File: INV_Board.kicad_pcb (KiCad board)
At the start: 2 copper layers, 100 x 50 mm, 109 parts, among them J1 USB_B_Micro, J10 Conn_01x02_Male, J11 Conn_01x04_Male, J2 Conn_01x02_Male, J3 Conn_01x02_Male, J4 Conn_01x02_Male, J5 Conn_01x04_Male, J6 Conn_01x03_Male, J7 Conn_01x03_Male, J8 Conn_ARM_JTAG_SWD_10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

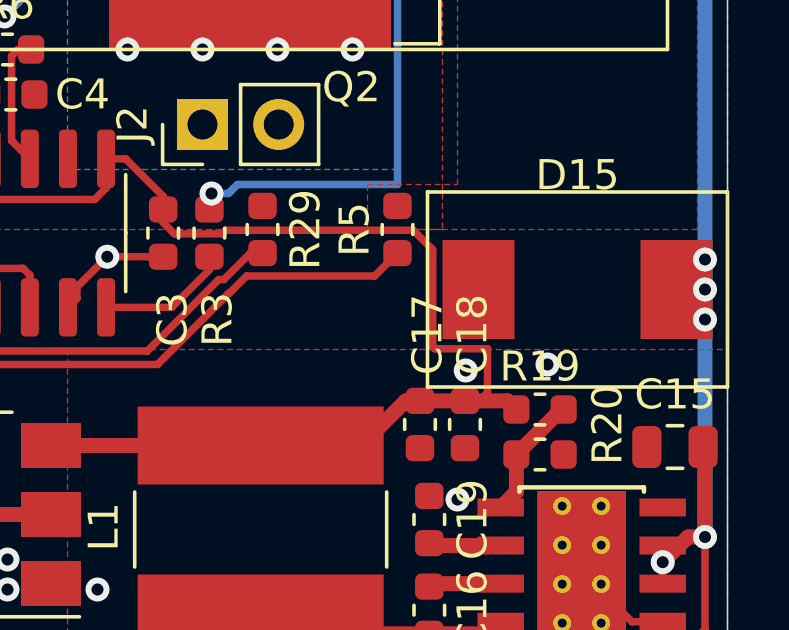
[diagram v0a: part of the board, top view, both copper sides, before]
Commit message: Commit changes to put omitted Vias on TVS ground.
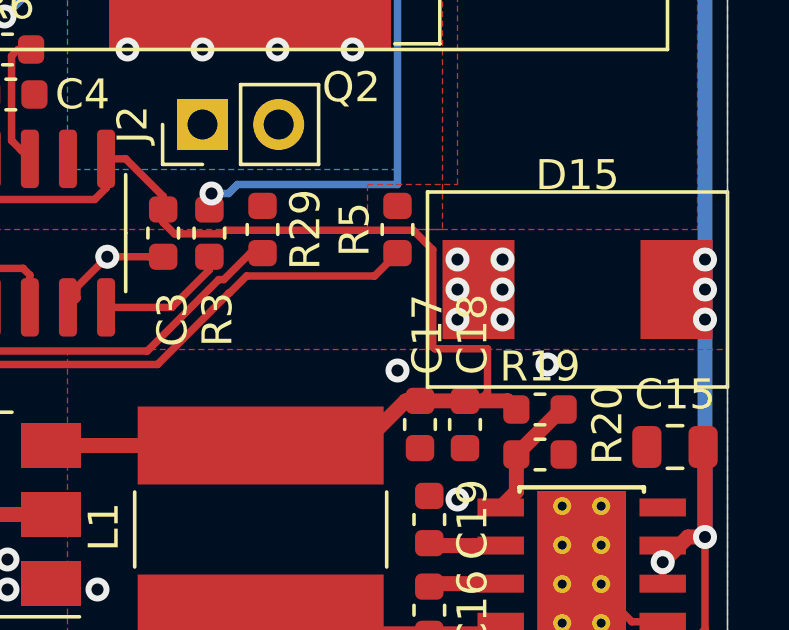
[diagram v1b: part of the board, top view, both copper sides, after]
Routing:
- net GND: vias 59 -> 65

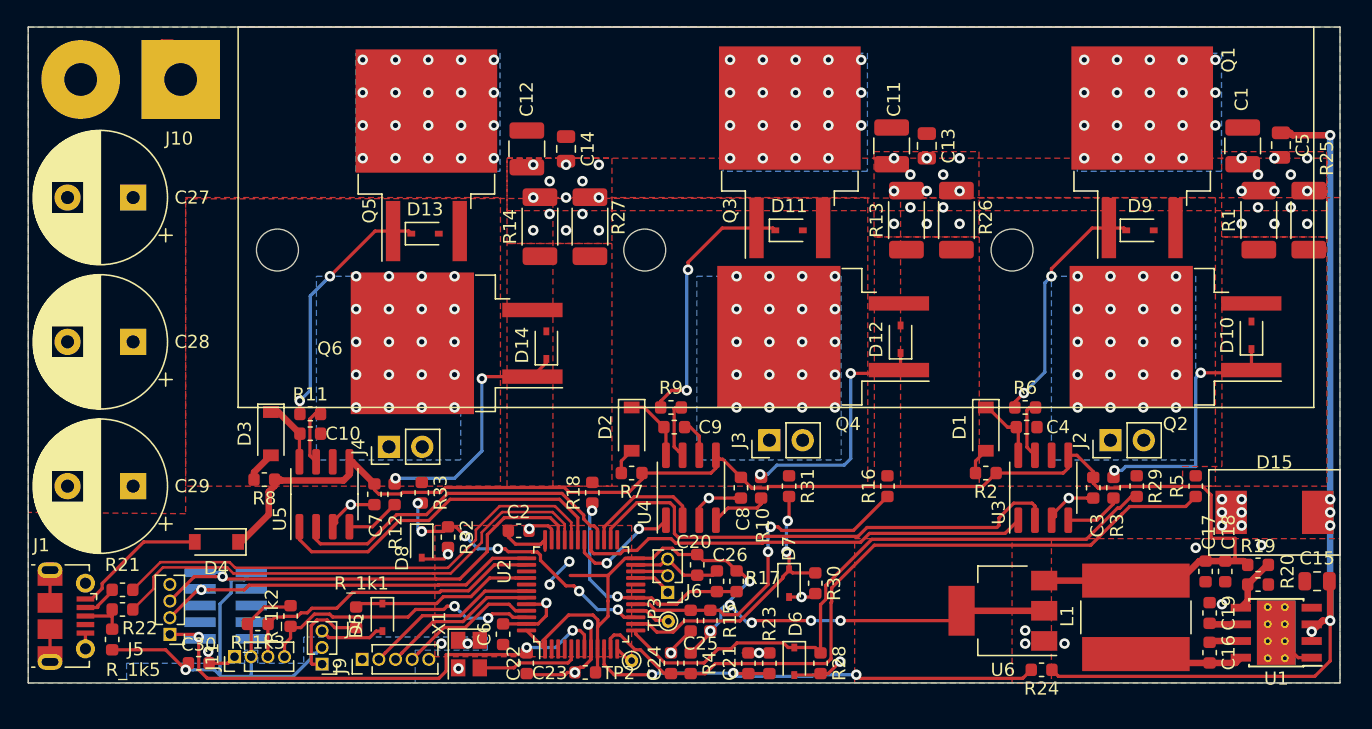
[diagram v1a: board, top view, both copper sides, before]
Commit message: Updates to add extra ceramic caps on power line next to FETs, move high frequency 0805 capacitor to closest position next to FETs, move shunts in a fewmm to reduce inductive current loops, update schematic pinout diagram.
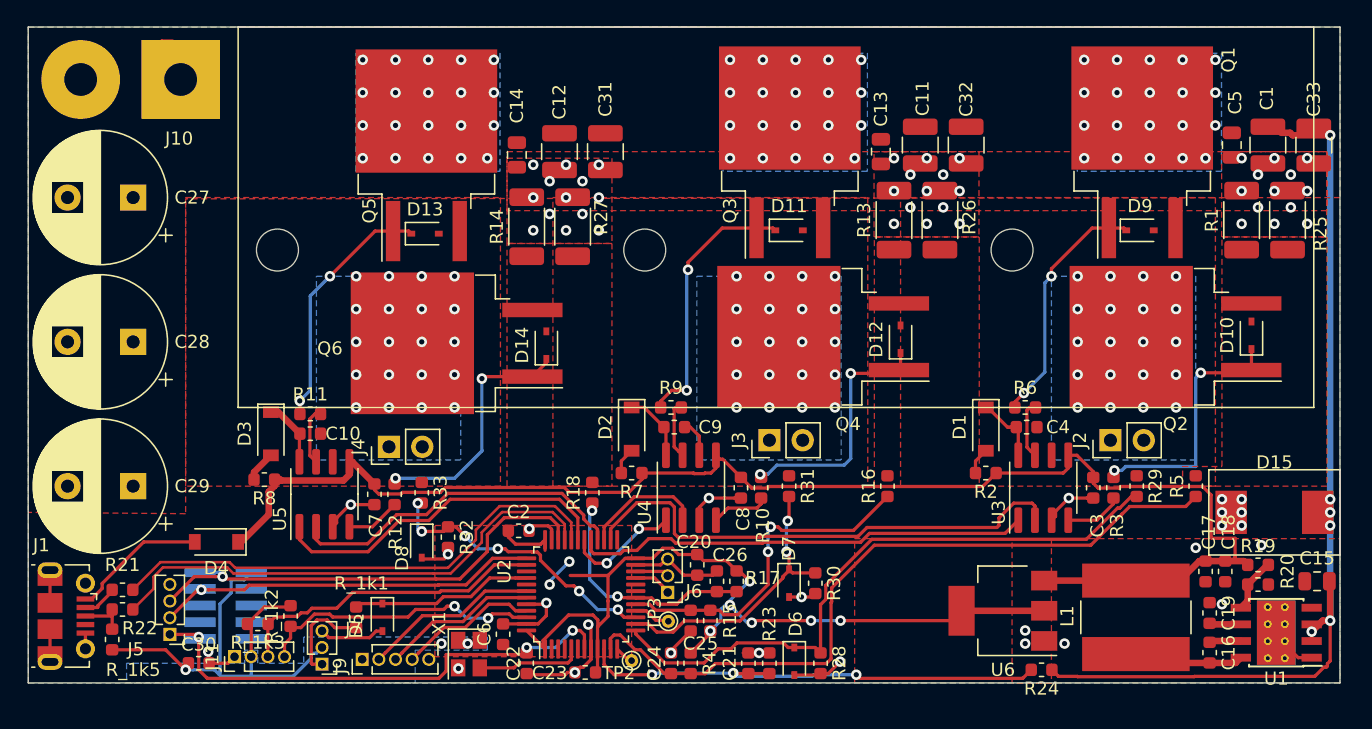
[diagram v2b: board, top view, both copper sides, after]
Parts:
- added C31: C_10uF 75V, Capacitor_SMD:C_1210_3225Metric, F.Cu at (84.0, 37.5)
- added C32: C_10uF 75V, Capacitor_SMD:C_1210_3225Metric, F.Cu at (111.5, 37.0)
- added C33: C_10uF 75V, Capacitor_SMD:C_1210_3225Metric, F.Cu at (138.0, 37.0)
- moved C14 3.78 mm to (77.2, 37.8)
- moved C5 3.75 mm to (131.8, 37.0)
- moved C13 3.53 mm to (105.0, 37.5)
- moved C12 2.50 mm to (80.5, 37.5)
- moved C11 2.18 mm to (108.0, 37.0)
- moved C1 1.92 mm to (134.5, 37.0)
- moved R25 1.62 mm to (136.0, 42.7)
- moved R27 1.32 mm to (81.5, 43.2)
- moved R1 1.31 mm to (132.5, 42.7)
- moved R26 1.26 mm to (109.5, 42.7)
- moved R14 1.01 mm to (78.0, 43.2)
- moved R13 0.95 mm to (106.0, 42.7)
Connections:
- net Net-(U2-Pad19) renamed /op3Vout
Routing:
- net +VDC: track 73.0 -> 73.1 mm, vias 64 -> 66
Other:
- net class HV added: clearance 0.2, trace_width 0.25, via_dia 0.8, via_drill 0.4

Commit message: Update to add 5V rail using TPS560430, smaller 3v3 reg, 3v3 pullups and 5V power on hall sensors, tidy up the schematic a bit.
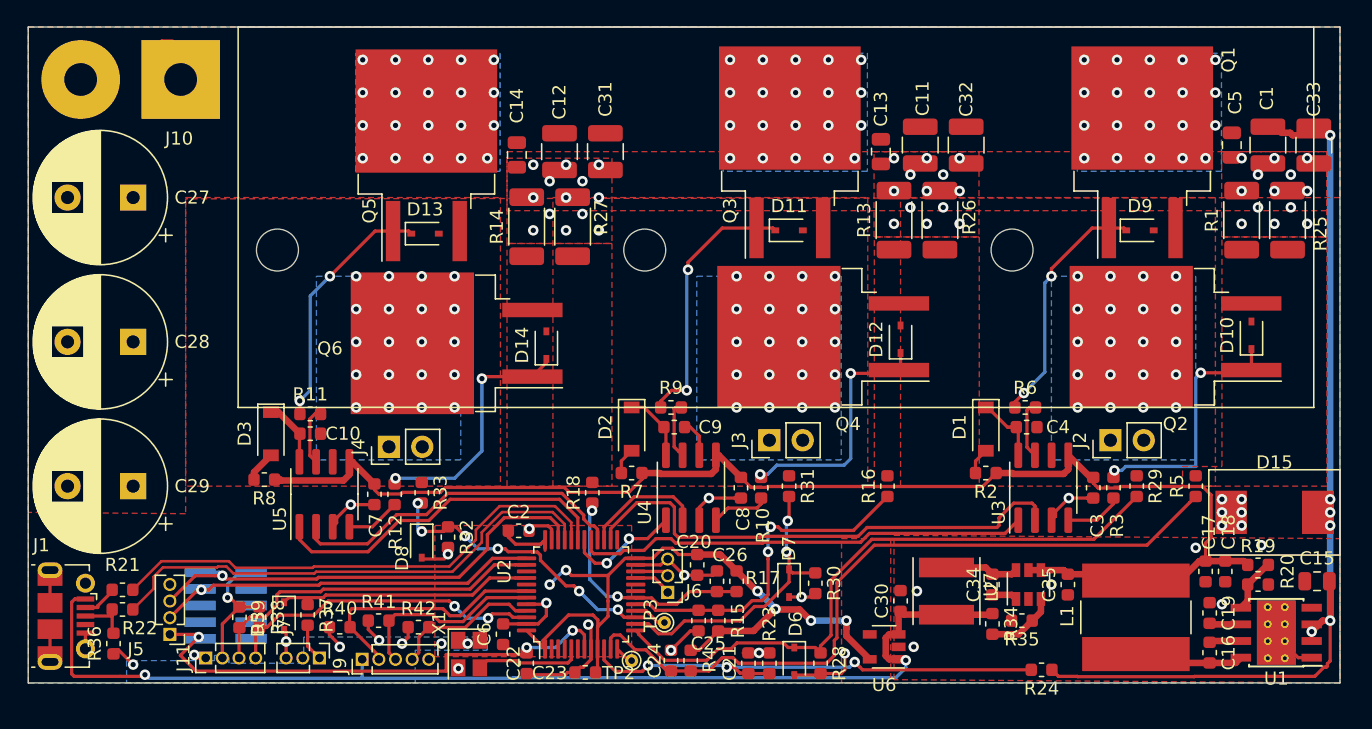
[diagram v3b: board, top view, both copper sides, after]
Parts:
- removed D4: D_Schottky, Diode_SMD:D_SOD-123
- removed R_1k1, R_1k2, R_1k3, R_1k5: R_5, Resistor_SMD:R_0603_1608Metric
- added C34: C_0.1uF_25V, Capacitor_SMD:C_0603_1608Metric, F.Cu at (113.5, 70.5)
- added C35: C_0.1uF_25V, Capacitor_SMD:C_0603_1608Metric, F.Cu at (119.2, 70.5)
- added L2: L_15uH_1A, Inductor_SMD:L_Taiyo-Yuden_NR-50xx, F.Cu at (110.0, 71.0)
- added R34: R_47k, Resistor_SMD:R_0603_1608Metric, F.Cu at (113.5, 73.5)
- added R35: R_12k, Resistor_SMD:R_0603_1608Metric, F.Cu at (115.8, 73.2)
- added R36: R_1k5, Resistor_SMD:R_0603_1608Metric, F.Cu at (46.5, 75.0)
- added R37: R_1k5, Resistor_SMD:R_0603_1608Metric, F.Cu at (61.3, 72.8)
- added R38: R_1k5, Resistor_SMD:R_0603_1608Metric, F.Cu at (57.6, 73.0)
- added R39: R_1k5, Resistor_SMD:R_0603_1608Metric, F.Cu at (56.1, 73.0)
- added R40: R_1k5, Resistor_SMD:R_0603_1608Metric, F.Cu at (63.8, 73.8)
- added R41: R_1k5, Resistor_SMD:R_0603_1608Metric, F.Cu at (66.7, 73.2)
- added R42: R_1k5, Resistor_SMD:R_0603_1608Metric, F.Cu at (69.8, 73.8)
- added U7: TPS560430, Package_TO_SOT_SMD:SOT-23-6, F.Cu at (116.2, 70.5)
- C13, C14, C15, C5: value C_Small -> C_0.1uF_100V
- C22: value C_1uF_25V -> C_0.1uF_25V
- D10, D11, D12, D13, D14, D9: value D_Zener_Small -> D_Zener_16V
- D5, D6, D7, D8: value D_Zener_Small -> D_Zener_3v3
- L1: value L_Small -> L_100uH_1.5A
- R1, R13, R14, R25, R26, R27: value R_Shunt -> R_Shunt_2mR
- U6: value LM1117-3.3 -> TPS76333; footprint Package_TO_SOT_SMD:SOT-223-3_TabPin2 -> Package_TO_SOT_SMD:SOT-23-5
- moved C30 53.7 mm to (106.5, 71.8), turned to 90 degrees
- moved U6 9.46 mm to (105.2, 75.2)
- moved D5 7.50 mm to (59.5, 72.9)
- moved J11 2.20 mm to (53.5, 76.1)
- moved C25 0.60 mm to (91.1, 73.2)
- moved R15 0.60 mm to (92.6, 73.2)
- moved J7 0.51 mm to (62.2, 76.1), turned to 270 degrees
- moved TP3 0.32 mm to (88.5, 73.4)
- moved C24 0.20 mm to (89.0, 76.3)
- moved R4 0.20 mm to (90.5, 76.3)
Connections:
- C30 pad 1: +3V3 -> +5V
- J1 pad 1: Net-(D4-Pad2) -> +5V
- J9 pad 1: +3V3 -> +5V
- U6 pad 1: GND -> +5V
- U6 pad 2: +3V3 -> GND
- U6 pad 3: +10V -> +5V
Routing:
- net +5V: track 0.00 -> 85.9 mm, vias 0 -> 2
- net +3V3: track 106.8 -> 76.1 mm, vias 11 -> 13
- net Net-(D4-Pad2): track 10.4 -> 0.00 mm
- net +10V: track 110.2 -> 104.1 mm
- net PWMin: track 13.9 -> 19.8 mm
- net /Hall1: track 13.4 -> 19.2 mm
- net Net-(C34-Pad2): track 0.00 -> 5.64 mm
- net Net-(R34-Pad2): track 0.00 -> 5.39 mm
- net Net-(J7-Pad1): track 7.56 -> 2.87 mm
- net GND: track 68.2 -> 65.1 mm, vias 65 -> 66
- net /Hall2: track 11.9 -> 14.7 mm
- net I2CSCL: track 24.1 -> 26.7 mm
- net I2CSDA: track 22.0 -> 24.5 mm
- net Net-(C34-Pad1): track 0.00 -> 1.93 mm
- net #RES: track 38.0 -> 38.9 mm
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
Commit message: Tidied up schematic, added snubber pads using 0805 cap and resistor as close as possible to FETs (courtyards infringed, but this is intentional to improve performance), added ferrite bead in front of LMR35610 to damp noise, and allow for seperate powering of LMR if required by not fitting ferrite. This would enable voltages limited only by the MOSFETs and capacitors fitted.
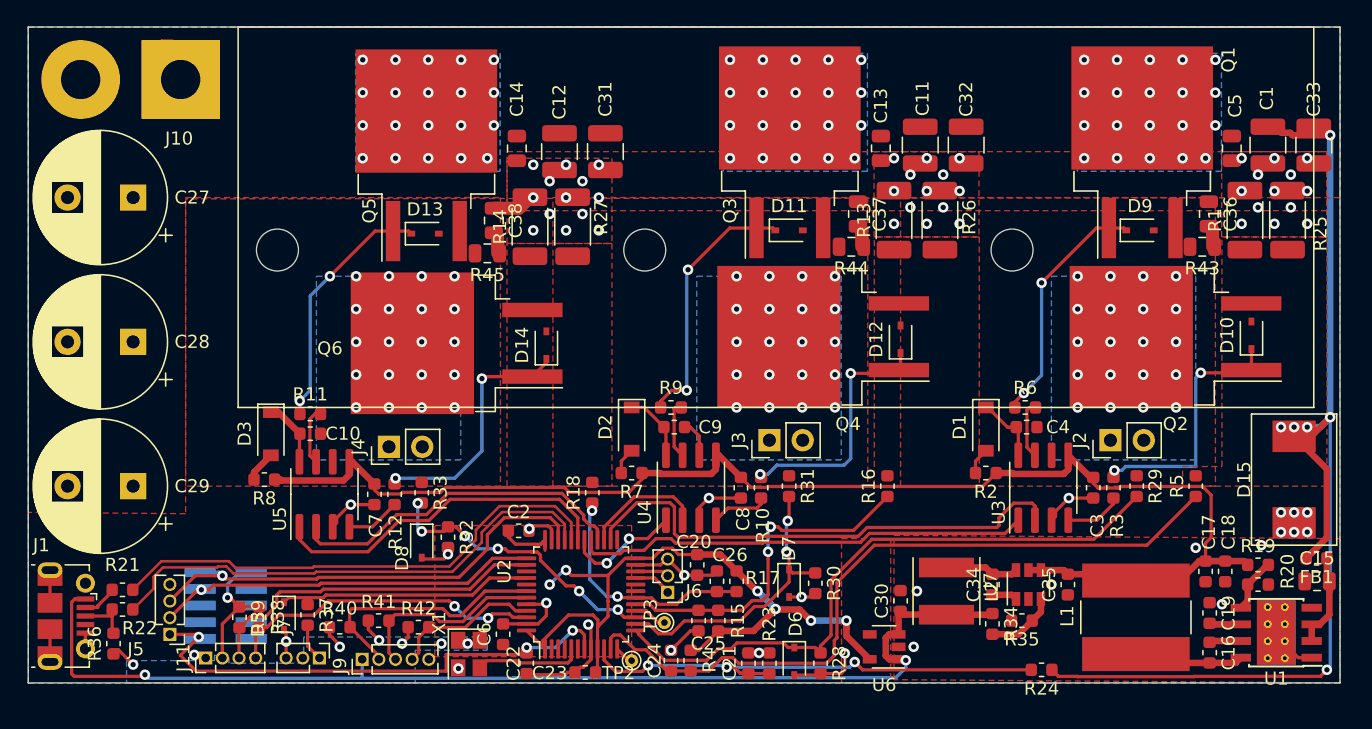
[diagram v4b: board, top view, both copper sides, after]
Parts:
- added C36: C_0.01uF_100V, Capacitor_SMD:C_0805_2012Metric, F.Cu at (130.0, 42.2)
- added C37: C_0.01uF_100V, Capacitor_SMD:C_0805_2012Metric, F.Cu at (103.2, 42.2)
- added C38: C_0.01uF_100V, Capacitor_SMD:C_0805_2012Metric, F.Cu at (75.5, 42.8)
- added FB1: Ferrite_Bead_Small, Resistor_SMD:R_0603_1608Metric, F.Cu at (138.2, 68.5)
- added R43: R_1, Resistor_SMD:R_0805_2012Metric, F.Cu at (129.5, 44.8)
- added R44: R_1, Resistor_SMD:R_0805_2012Metric, F.Cu at (102.8, 44.8)
- added R45: R_1, Resistor_SMD:R_0805_2012Metric, F.Cu at (75.0, 45.2)
- moved D15 2.92 mm to (136.5, 62.5), turned to 270 degrees
- moved C14 0.50 mm to (77.2, 37.2)
- moved C13 0.25 mm to (105.0, 37.2)
- moved C5 0.25 mm to (131.8, 37.2)
- moved R1 0.25 mm to (132.8, 42.7)
- moved R14 0.25 mm to (78.2, 43.2)
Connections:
- C15 pad 1: +VDC -> Net-(C15-Pad1)
- U1 pad 2: +VDC -> Net-(C15-Pad1)
- U1 pad 3: +VDC -> Net-(C15-Pad1)
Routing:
- net +VDC: track 73.1 -> 85.6 mm
- net Net-(C15-Pad1): track 0.00 -> 8.66 mm
- net GND: track 65.1 -> 68.2 mm
- net Net-(C38-Pad2): track 0.00 -> 1.68 mm
- net Net-(C37-Pad2): track 0.00 -> 1.68 mm
- net Net-(C36-Pad2): track 0.00 -> 1.68 mm

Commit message: Change power scheme to have 5V rail genreated from LMR36510, and then boost it up to 12V for the gate drivers, which use very little power. This scheme allows the use of a seperate power source for the MCU and gate drives, enabling the use of the system up to the limits of gate drive and MOSFETs. Added notes for the connections to make it easier to use.
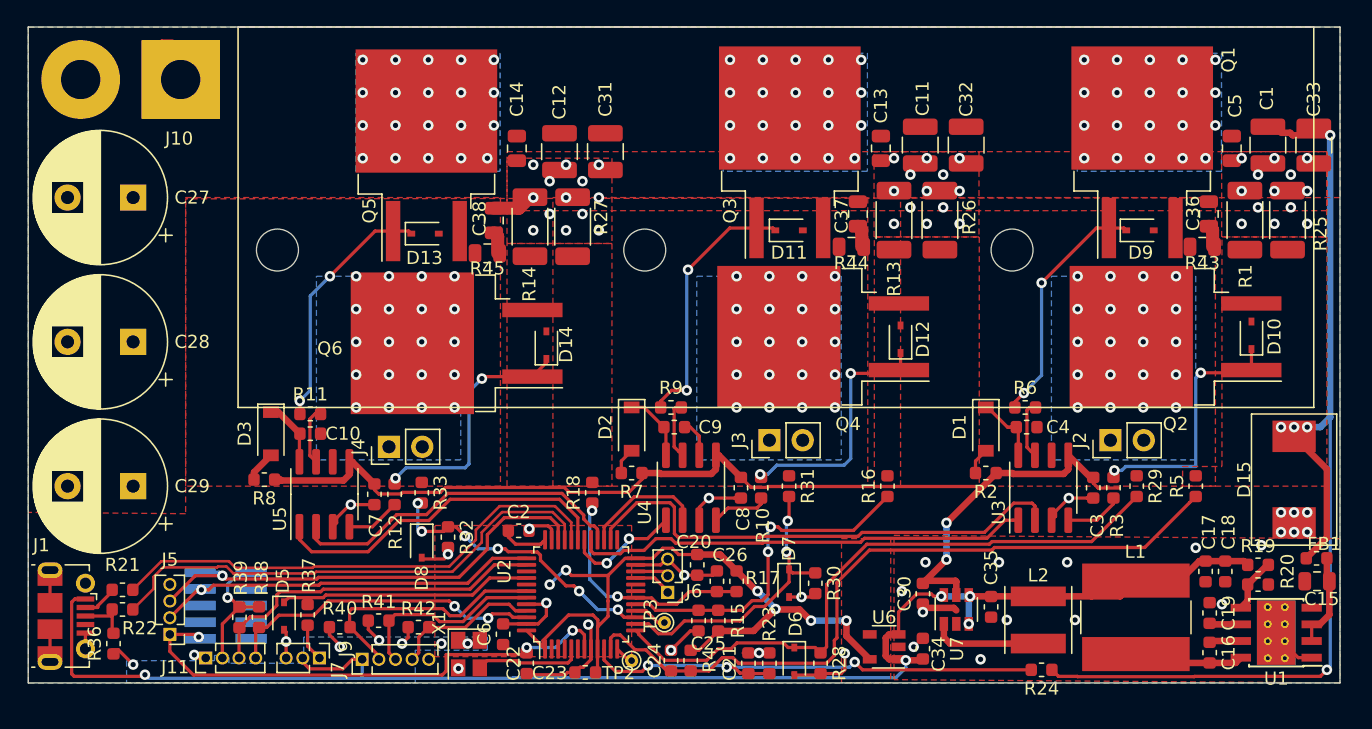
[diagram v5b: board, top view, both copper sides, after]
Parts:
- removed R34: R_47k, Resistor_SMD:R_0603_1608Metric
- removed R35: R_12k, Resistor_SMD:R_0603_1608Metric
- C27, C28, C29: value CP_Small -> CP_220uF
- C34: value C_0.1uF_25V -> C_1uF_25V
- R19: value R_47k -> R_18k
- U7: value TPS560430 -> TLV61046ADB
- moved L2 7.34 mm to (117.0, 73.2)
- moved C34 7.21 mm to (108.2, 75.4)
- moved C35 6.09 mm to (113.4, 72.2)
- moved U7 5.82 mm to (110.8, 72.4)
- moved C30 1.79 mm to (108.2, 71.2), turned to 270 degrees
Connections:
- C17 pad 1: +10V -> +5V
- C18 pad 1: +10V -> +5V
- C3 pad 1: +10V -> +12V
- C30 pad 1: +5V -> +12V
- C34 pad 1: Net-(C34-Pad1) -> +5V
- C34 pad 2: Net-(C34-Pad2) -> GND
- C35 pad 2: +10V -> +5V
- C7 pad 1: +10V -> +12V
- C8 pad 1: +10V -> +12V
- J7 pad 2: +3V3 -> +5V
- L1 pad 2: +10V -> +5V
- L2 pad 1: Net-(C34-Pad2) -> +5V
- L2 pad 2: +5V -> Net-(L2-Pad2)
- R19 pad 1: +10V -> +5V
- R2 pad 1: +10V -> +12V
- R7 pad 1: +10V -> +12V
- R8 pad 1: +10V -> +12V
- U3 pad 5: +10V -> +12V
- U4 pad 5: +10V -> +12V
- U5 pad 5: +10V -> +12V
- U7 pad 1: Net-(C34-Pad1) -> Net-(L2-Pad2)
- U7 pad 3: Net-(R34-Pad2) -> +5V
- U7 pad 4: +10V -> +5V
- U7 pad 5: +10V -> +12V
- U7 pad 6: Net-(C34-Pad2) -> +5V
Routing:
- net +10V: track 104.1 -> 0.00 mm
- net +12V: track 0.00 -> 88.1 mm, vias 0 -> 2
- net +5V: track 85.9 -> 121.1 mm, vias 2 -> 5
- net Net-(L2-Pad2): track 0.00 -> 8.42 mm
- net Net-(C34-Pad2): track 5.64 -> 0.00 mm
- net Net-(R34-Pad2): track 5.39 -> 0.00 mm
- net GND: track 68.2 -> 70.4 mm, vias 66 -> 72
- net +VDC: track 85.6 -> 83.5 mm, vias 66 -> 65
- net Net-(C34-Pad1): track 1.93 -> 0.00 mm
- net Net-(C15-Pad1): track 8.66 -> 7.39 mm
- net +3V3: track 76.1 -> 75.3 mm
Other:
- board text added: "#Res SWC SWDIO G"
- board text added: "5V H1 H2 H3 G"
- board text added: "Cortex 10Pin Header"
- board text added: "G 3v3 SCL SDA"
- board text added: "G 5V PWM"
- board text added: "GND VDC"
- board text added: "I_PhU TP"
- board text added: "I_PhV TP"
- board text added: "PhU"
- board text added: "PhV"
- board text added: "PhW"
- board text added: "Tx Rx G"
- board text added: "USB B Micro"
